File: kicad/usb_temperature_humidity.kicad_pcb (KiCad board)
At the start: 2 copper layers, 72 x 47.5 mm, 15 parts, among them SW1 SW_SPDT, SW2 SW_SPDT, U1 SeeeduinoXIAO, U2 SHT-31, U3 PinHeader_XIAO, U4 PinHeader_XIAO, U5 SHT-31_aliexpress

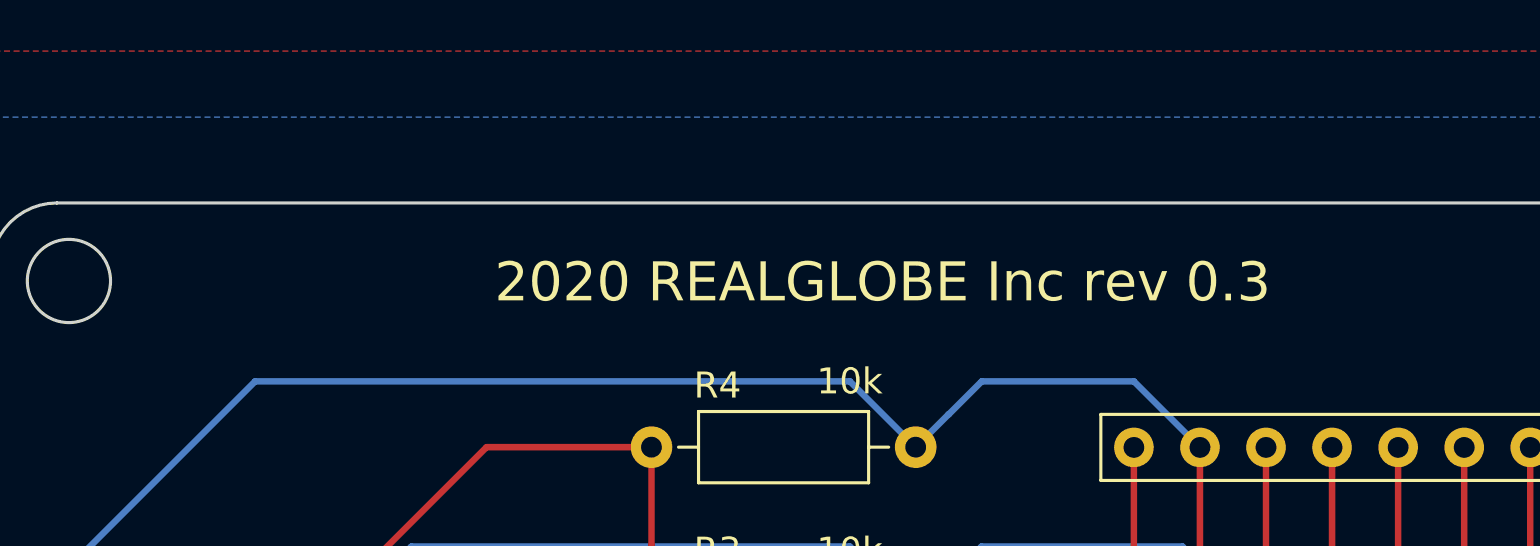
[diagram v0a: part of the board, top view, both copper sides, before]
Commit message: 基板上の署名をkoinoにした
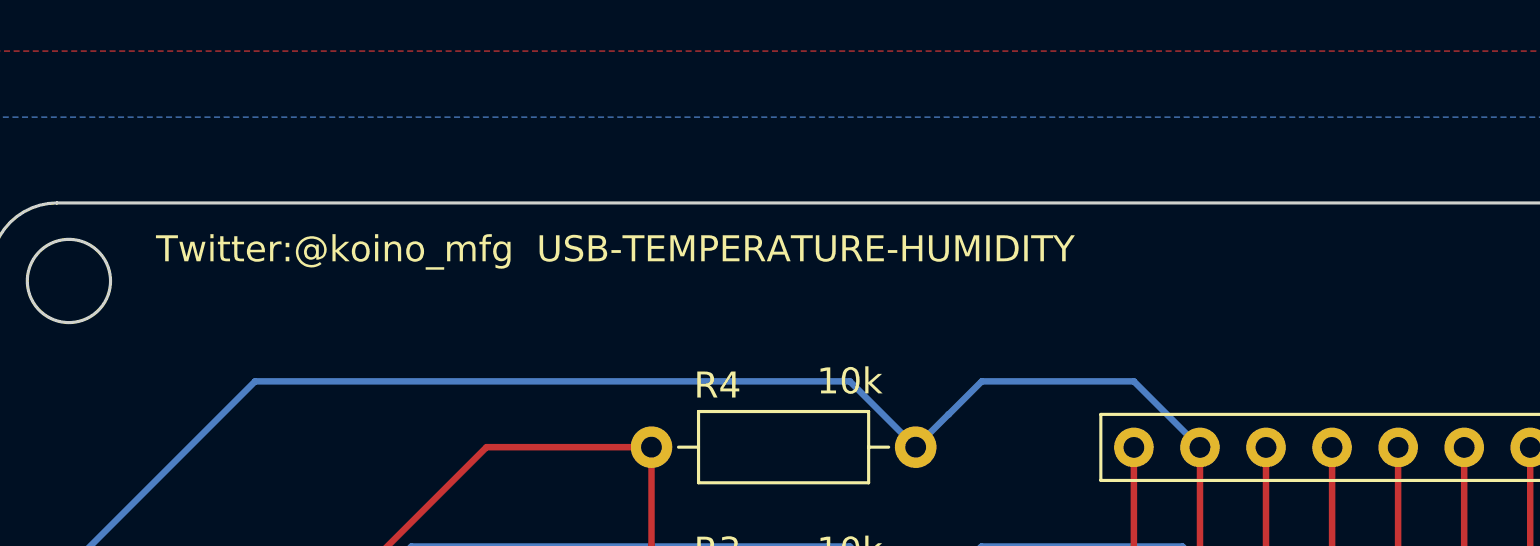
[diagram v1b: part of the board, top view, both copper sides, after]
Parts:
- added ~: signature_koino, kicad_mylib:signature_koino, F.Cu at (6.35, -44.5)
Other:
- board text removed: "2020 REALGLOBE Inc rev 0.3"
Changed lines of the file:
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@@
   (general
     (thickness 1.6)
-    (drawings 26)
+    (drawings 25)
     (tracks 105)
     (zones 0)
-    (modules 15)
+    (modules 16)
     (nets 27)
   )
@@
     (add_net "Net-(U5-Pad5)")
     (add_net "Net-(U5-Pad6)")
+  )
+  (module kicad_mylib:signature_koino (layer F.Cu)
+    (at 6.35 -44.45)
+    (fp_text reference ~ (at 2.54 -3.81) (layer F.SilkS)
+      (effects (font (size 1 1) (thickness 0.15)))
+    )
+    (fp_text value signature_koino (at 6.35 -5.58) (layer F.Fab)
+      (effects (font (size 1 1) (thickness 0.15)))
+    )
+    (fp_text user "Twitter:@koino_mfg  USB-TEMPERATURE-HUMIDITY" (at 0 -1.27) (layer F.SilkS)
+      (effects (font (size 1 1) (thickness 0.15)) (justify left))
+    )
   )
   (module Resistor_THT:R_Axial_DIN0207_L6.3mm_D2.5mm_P10.16mm_Horizontal (layer F.Cu)
@@
     (effects (font (size 1 1) (thickness 0.15)))
   )
-  (gr_text "2020 REALGLOBE Inc rev 0.3" (at 34.29 -44.45) (layer F.SilkS)
-    (effects (font (size 1.5 1.5) (thickness 0.3)))
-  )
   (gr_line (start 62.23 -33) (end 72 -33) (layer Edge.Cuts) (width 0.12))
